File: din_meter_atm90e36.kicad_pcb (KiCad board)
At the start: 4 copper layers, 32 x 31.1 mm, 72 parts, among them IC1 ATM90E36_ATM90E36, IC2 ATM90E36_ATM90E36, J7 Conn_01x10, J8 Conn_02x18_Row_Letter_First, Y1 Crystal_GND24, Y2 Crystal_GND24

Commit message: Add manufacturer number and more details on silk
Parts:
- added G1: LOGO, Whatnick_logo:Whatnick_logo, B.Cu at (138.7, 74.8)
- added G2: Logo_Open_Hardware_Small, Symbols:OSHW-Logo2_7.3x6mm_SilkScreen, B.Cu at (157.6, 65.4)
- added SYM1: SYM_Flash_Small, Whatnick_logo:Fsilk_HV, B.Cu at (153.5, 75.9)
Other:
- board text added: "Dual ATM90E36 Metering v0.3 23/02/2018"
- board text added: "TAPR"
- board text removed: "Dual ATM90E36 Metering v0.2 10/02/2018"

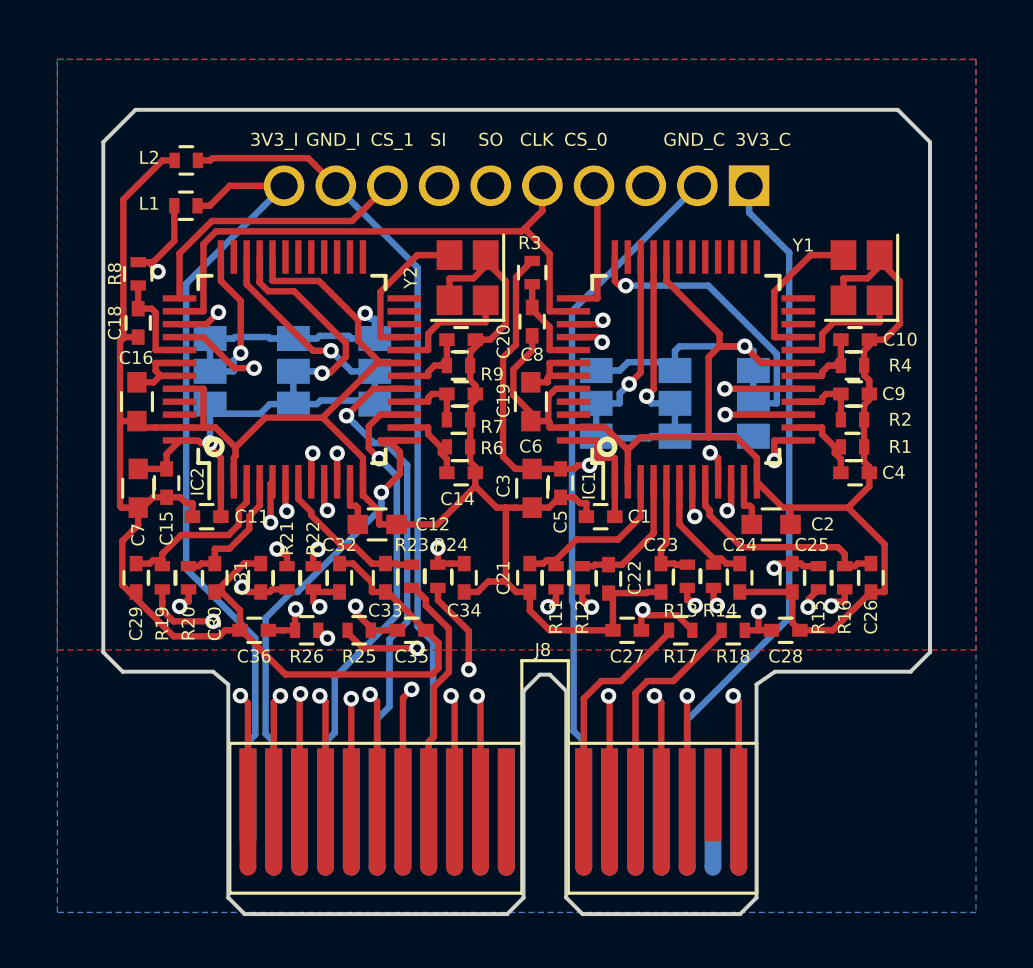
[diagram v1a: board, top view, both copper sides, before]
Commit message: Added step file and proper soldermask to open PCI-E connector
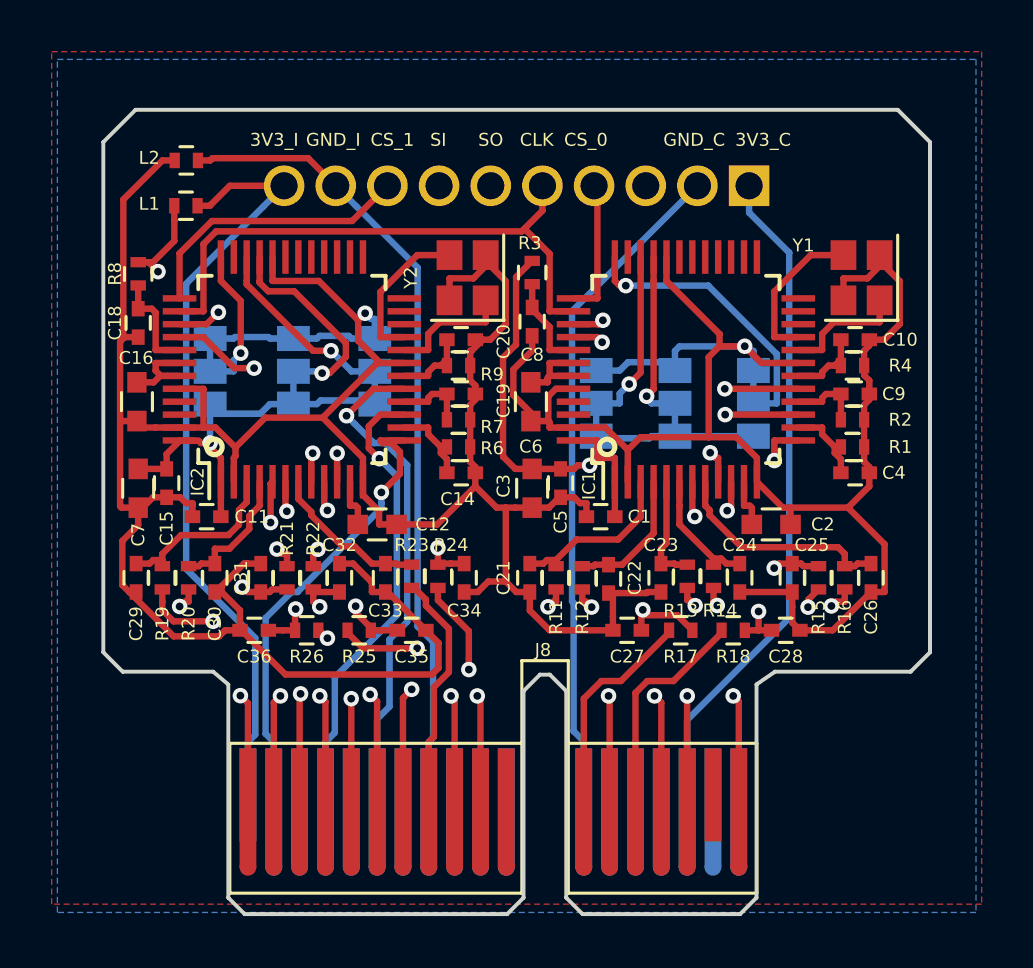
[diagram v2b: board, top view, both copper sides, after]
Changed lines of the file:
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@@
   (page A4)
   (layers
-    (0 F.Cu mixed hide)
+    (0 F.Cu mixed)
     (1 In1.Cu signal hide)
     (2 In2.Cu signal hide)
-    (31 B.Cu mixed hide)
+    (31 B.Cu mixed)
     (32 B.Adhes user)
     (33 F.Adhes user)
@@
     (37 F.SilkS user)
     (38 B.Mask user hide)
-    (39 F.Mask user hide)
+    (39 F.Mask user)
     (40 Dwgs.User user)
     (41 Cmts.User user)
@@
   (module Connectors:PCI-EXPRESS locked (layer F.Cu)
     (at 135.508 84.923)
-    (solder_mask_margin 1.6)
     (attr virtual)
     (fp_text reference J8 (at 11.418 -5.613) (layer F.SilkS)
@@
     (pad 48 smd rect (at -2.75 -4.35 180) (size 1.3 0.25) (layers F.Cu F.Paste F.Mask)
       (net 2 +3V3))
-    (model ${KISYS3DMOD}/Housings_QFP.3dshapes/TQFP-48_7x7mm_Pitch0.5mm.wrl
+    (model ${KISYS3DMOD}/Package_QFP.3dshapes/TQFP-48_7x7mm_P0.5mm.step
       (at (xyz 0 0 0))
       (scale (xyz 1 1 1))
@@
     (pad 1 smd rect (at -4.35 -2.75 90) (size 1.3 0.25) (layers F.Cu F.Paste F.Mask)
       (net 2 +3V3))
-    (model ${KISYS3DMOD}/Housings_QFP.3dshapes/TQFP-48_7x7mm_Pitch0.5mm.wrl
+    (model ${KISYS3DMOD}/Package_QFP.3dshapes/TQFP-48_7x7mm_P0.5mm.step
       (at (xyz 0 0 0))
       (scale (xyz 1 1 1))
@@
     (polygon
       (pts
-        (xy 128.13 56.45) (xy 163.69 56.45) (xy 163.69 79.31) (xy 128.13 79.31)
+        (xy 127.91 56.15) (xy 163.91 56.15) (xy 163.91 89.15) (xy 127.91 89.15)
       )
     )
@@
       )
     )
+  )
+  (zone (net 0) (net_name "") (layer F.Mask) (hatch edge 0.508)
+    (connect_pads (clearance 0.2))
+    (min_thickness 0.254)
+    (fill yes (arc_segments 16) (thermal_gap 0.508) (thermal_bridge_width 0.508))
+    (polygon
+      (pts
+        (xy 133.91 83.15) (xy 155.91 83.15) (xy 155.91 90.15) (xy 133.91 90.15)
+      )
+    )
+  )
+  (zone (net 0) (net_name "") (layer B.Mask) (hatch edge 0.508)
+    (connect_pads (clearance 0.2))
+    (min_thickness 0.254)
+    (fill yes (arc_segments 16) (thermal_gap 0.508) (thermal_bridge_width 0.508))
+    (polygon
+      (pts
+        (xy 133.91 83.15) (xy 155.91 83.15) (xy 155.91 90.15) (xy 133.91 90.15)
+      )
+    )

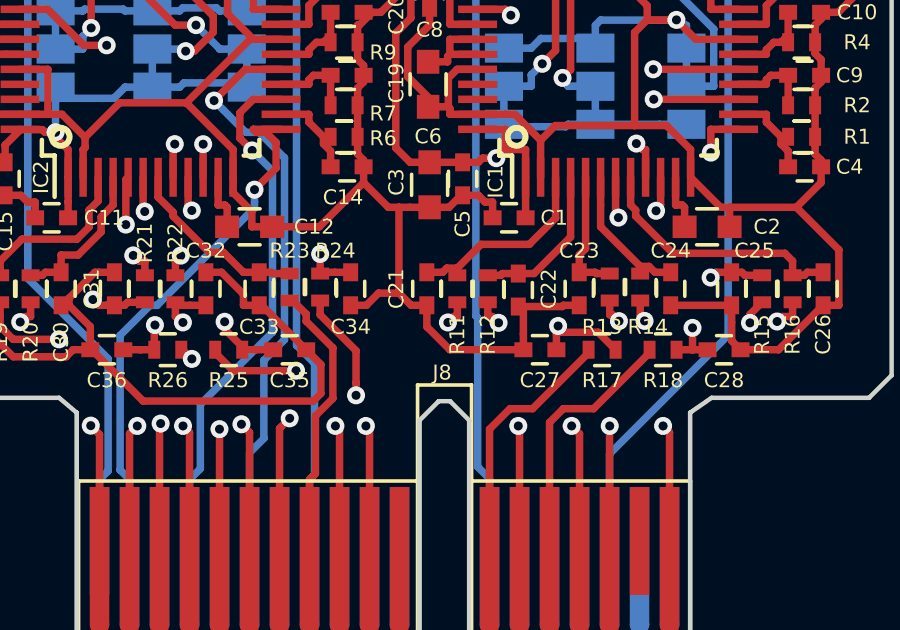
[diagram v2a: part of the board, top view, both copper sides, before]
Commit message: Fix a trace outside board edge
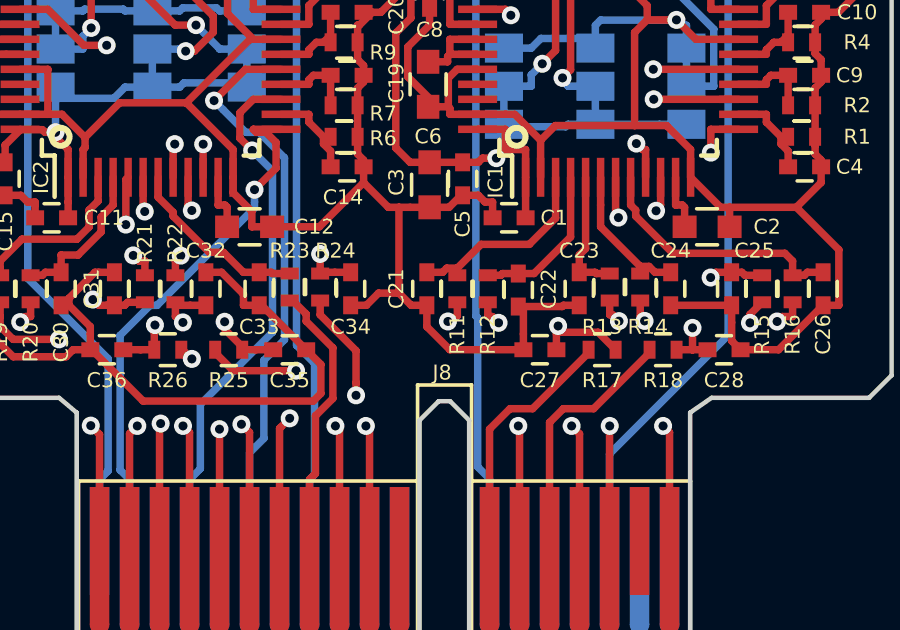
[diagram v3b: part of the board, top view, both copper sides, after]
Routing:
- net IC1-: track 27.1 -> 29.8 mm
